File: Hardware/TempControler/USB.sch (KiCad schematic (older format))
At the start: 5 parts, among them J3 USB_B_Micro

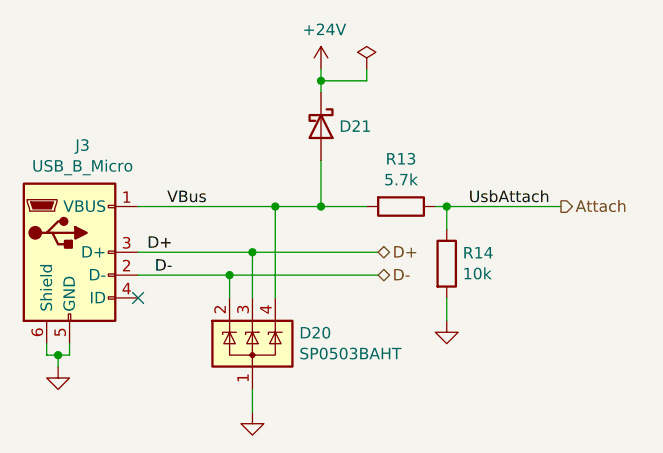
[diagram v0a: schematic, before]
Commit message: All Part Numbers Selected
Next step select all footprints
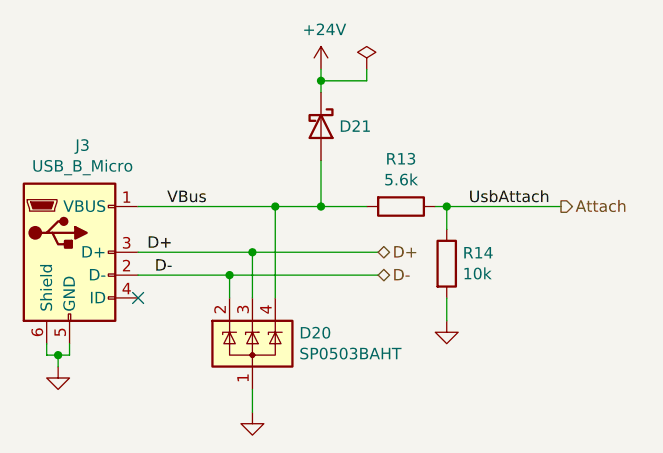
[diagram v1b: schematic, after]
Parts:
- D20: Mouser (none) -> 576-SP0503BAHTG
- D21: value D_Schottky -> RB080LAM-30TR; Mouser (none) -> 755-RB080LAM-30TR
- J3: Mouser (none) -> 649-10118194-0011LF
- R13: value 5.7k -> 5.6k; Mouser (none) -> 71-CRCW06035K60FKEAC
- R14: Mouser (none) -> 667-ERJ-3EKF1002V
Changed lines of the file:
@@
 F 1 "USB_B_Micro" H 1657 2826 50  0000 C CNN
 F 2 "misc:USB_Micro-B_Amphenol_10118194-0011LF_Horizontal" H 1750 2400 50  0001 C CNN
-F 3 "~" H 1750 2400 50  0001 C CNN
+F 3 "https://www.amphenol-icc.com/micro-usb-101181940011lf.html" H 1750 2400 50  0001 C CNN
+F 4 "649-10118194-0011LF" H 1600 2450 50  0001 C CNN "Mouser"
 	1    1600 2450
 	1    0    0    -1
@@
 P 3050 2250
 F 0 "R13" V 2843 2250 50  0000 C CNN
-F 1 "5.7k" V 2934 2250 50  0000 C CNN
+F 1 "5.6k" V 2934 2250 50  0000 C CNN
 F 2 "Resistor_SMD:R_0603_1608Metric" V 2980 2250 50  0001 C CNN
-F 3 "~" H 3050 2250 50  0001 C CNN
+F 3 "https://www.mouser.com/datasheet/2/427/crcwce3-1762584.pdf" H 3050 2250 50  0001 C CNN
+F 4 "71-CRCW06035K60FKEAC" H 3050 2250 50  0001 C CNN "Mouser"
 	1    3050 2250
 	0    1    1    0
@@
 F 1 "10k" H 3320 2455 50  0000 L CNN
 F 2 "Resistor_SMD:R_0603_1608Metric" V 3180 2500 50  0001 C CNN
-F 3 "~" H 3250 2500 50  0001 C CNN
+F 3 "https://www.mouser.com/datasheet/2/315/AOA0000C304-1149620.pdf" H 3250 2500 50  0001 C CNN
+F 4 "667-ERJ-3EKF1002V" H 3250 2500 50  0001 C CNN "Mouser"
 	1    3250 2500
 	1    0    0    -1
@@
 P 2700 1900
 F 0 "D21" V 2700 1980 50  0000 L CNN
-F 1 "D_Schottky" V 2745 1980 50  0001 L CNN
+F 1 "RB080LAM-30TR" V 2745 1980 50  0001 L CNN
 F 2 "Diode_SMD:D_SOD-128" H 2700 1900 50  0001 C CNN
-F 3 "~" H 2700 1900 50  0001 C CNN
+F 3 "https://www.mouser.com/datasheet/2/348/rb080lam_30tr_e-1869813.pdf" H 2700 1900 50  0001 C CNN
+F 4 "755-RB080LAM-30TR" H 2700 1900 50  0001 C CNN "Mouser"
 	1    2700 1900
 	0    1    1    0
@@
 F 2 "Package_TO_SOT_SMD:SOT-143" H 2625 2800 50  0001 L CNN
 F 3 "http://www.littelfuse.com/~/media/files/littelfuse/technical%20resources/documents/data%20sheets/sp05xxba.pdf" H 2525 2975 50  0001 C CNN
+F 4 "576-SP0503BAHTG" H 2400 2850 50  0001 C CNN "Mouser"
 	1    2400 2850
 	1    0    0    -1
